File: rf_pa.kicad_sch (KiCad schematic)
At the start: 57 parts, among them J1 LMT87LPM, Q1 BSS138, Q2 BSS138, Q3 NP100P04PDG, U1 LT1013DIDR, U2 LM317_SOT-223, U3 TL431, U4 RA60H3847H1

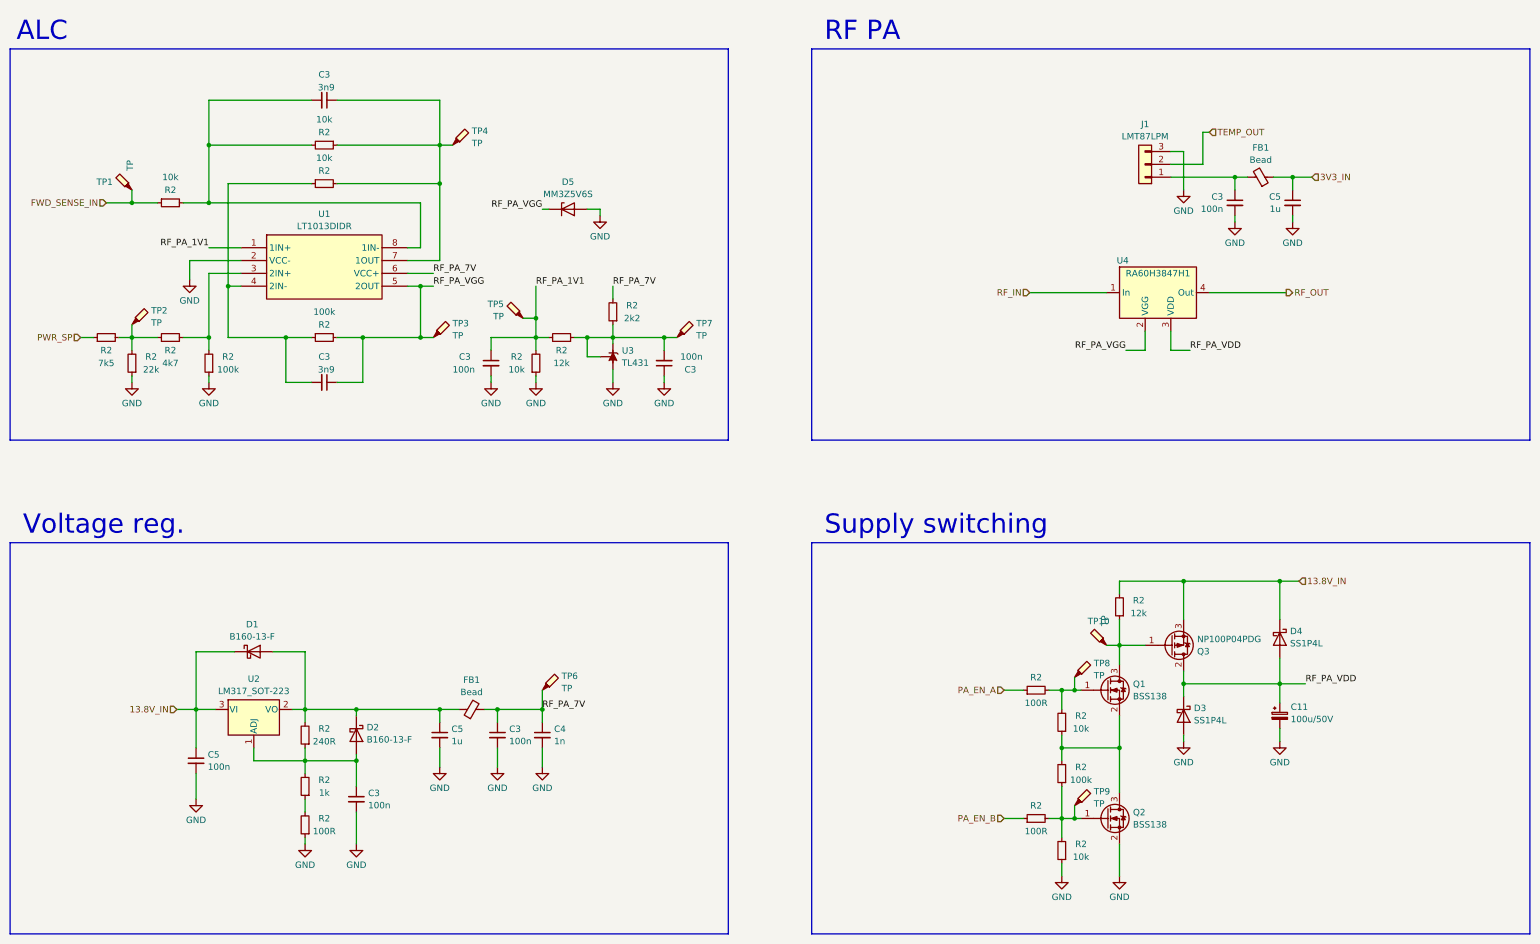
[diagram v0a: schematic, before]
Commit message: WIP rev B
- replaced R44-R46 with 22k
- exposed BOOT0 at the DA15 connector
- added a testpoint at DAC OUT2
- added a buffer to the 40MHz reference oscillator
- removed C2
- bypassed R5 with a 100nF capacitor
- changed D5's voltage to 5.1V
- routed TX_SAMP_CLK
- changed temperature sensor's supply voltage to 5V
- added a series of 100p, 1n and 10n capacitors at PA_VGG
- reduced N-connector cutouts to 2.5mm
- improved RF output track a little
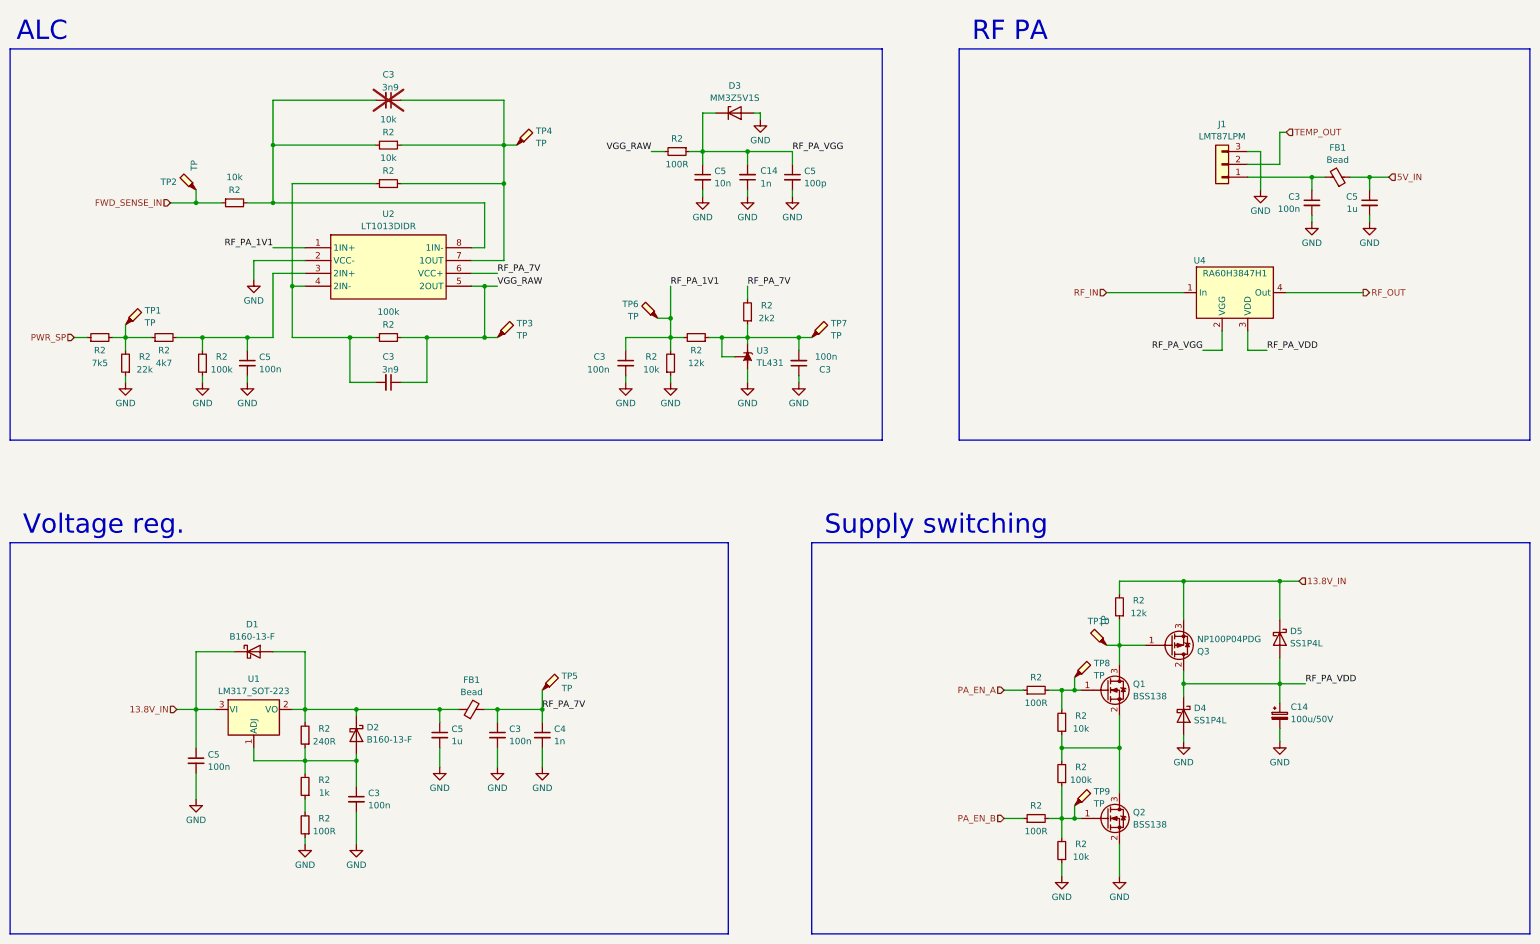
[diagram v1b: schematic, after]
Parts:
- added C14: 1n, Capacitor_SMD:C_0603_1608Metric, symbol Device:C_Small
- added C5: 10n, Capacitor_SMD:C_0603_1608Metric, symbol Device:C_Small
- added C5: 100p, Capacitor_SMD:C_0603_1608Metric, symbol Device:C_Small
- added C5: 100n, Capacitor_SMD:C_0603_1608Metric, symbol Device:C_Small
- added R2: 100R, Resistor_SMD:R_0603_1608Metric, symbol Device:R_Small
- C3: now not fitted; now left out of the parts list
- D3: renamed from D5; value MM3Z5V6S -> MM3Z5V1S; MPN MM3Z5V6ST1G -> 863-MM3Z5V1ST1G; PN MM3Z5V6ST1G -> 863-MM3Z5V1ST1G
- renumbered C11 to C14, D3 to D4, D4 to D5, TP2 to TP1, TP1 to TP2, TP6 to TP5, TP5 to TP6, U2 to U1, U1 to U2
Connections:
- net GND: now also C14.1, C5.2, C5.2, C5.2
- net RF_PA_VGG: now also C14.2, C5.1, C5.1, R2.1; no longer C3.1, R2.2, TP3.1, U2.5 (2OUT)
- net at R2.2, R2.2, U2.3 (2IN+): now also C5.1
- net 3V3_IN renamed 5V_IN
- new net VGG_RAW: C3.1, R2.2, R2.2, TP3.1, U2.5 (2OUT)
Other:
- moved on the sheet: C3, C5, D3, FB1, J1, R2, TP1, TP2, TP3, TP4, TP6, TP7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

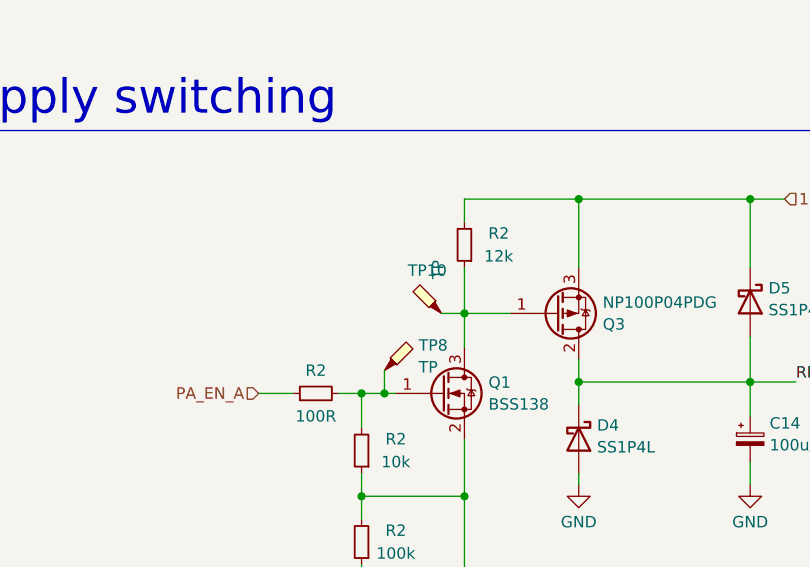
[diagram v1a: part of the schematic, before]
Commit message: routed the 40MHz oscillator
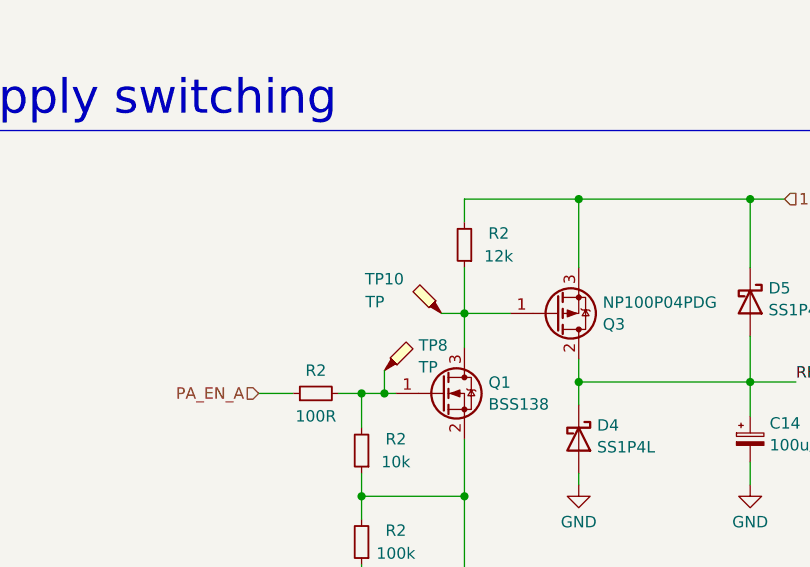
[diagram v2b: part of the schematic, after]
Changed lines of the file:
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@@
   )
   (symbol (lib_id "Connector:TestPoint_Probe") (at 271.78 175.26 90) (unit 1)
-    (in_bom yes) (on_board yes) (dnp no) (fields_autoplaced)
-    (property "Reference" "TP10" (at 270.1925 170.4919 90)
+    (in_bom yes) (on_board yes) (dnp no)
+    (property "Reference" "TP10" (at 265.43 171.45 90)
       (effects (font (size 1.27 1.27)))
     )
-    (property "Value" "TP" (at 271.4046 171.45 0)
+    (property "Value" "TP" (at 265.43 173.99 90)
       (effects (font (size 1.27 1.27)) (justify left))
     )

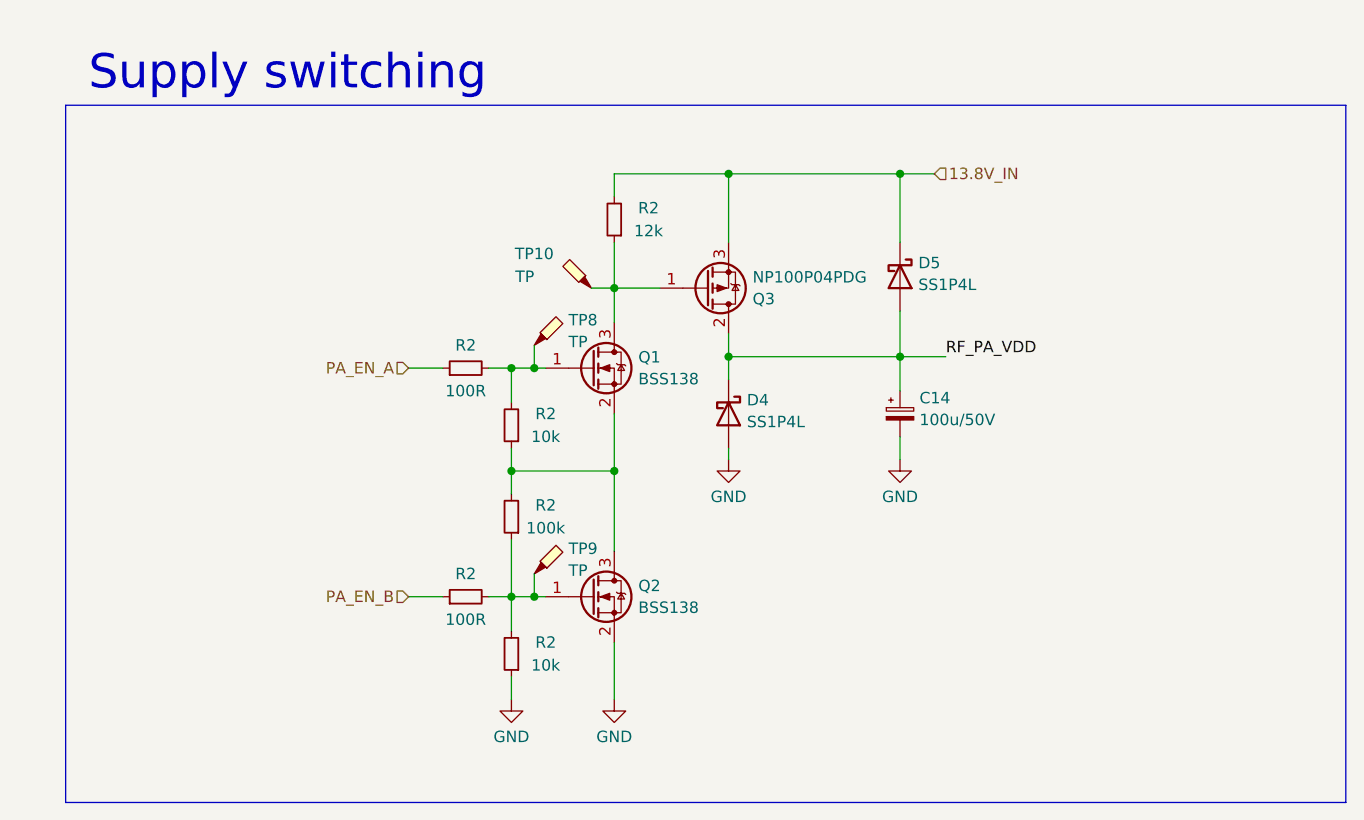
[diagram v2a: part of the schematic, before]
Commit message: WIP rev B
- added bleed resistors
- power supply now uses linear regulators
- routed RX_SAMP_CLK
- added some decoupling at RF_PA_VDD
- added some GND vias here and there
- updated BOM
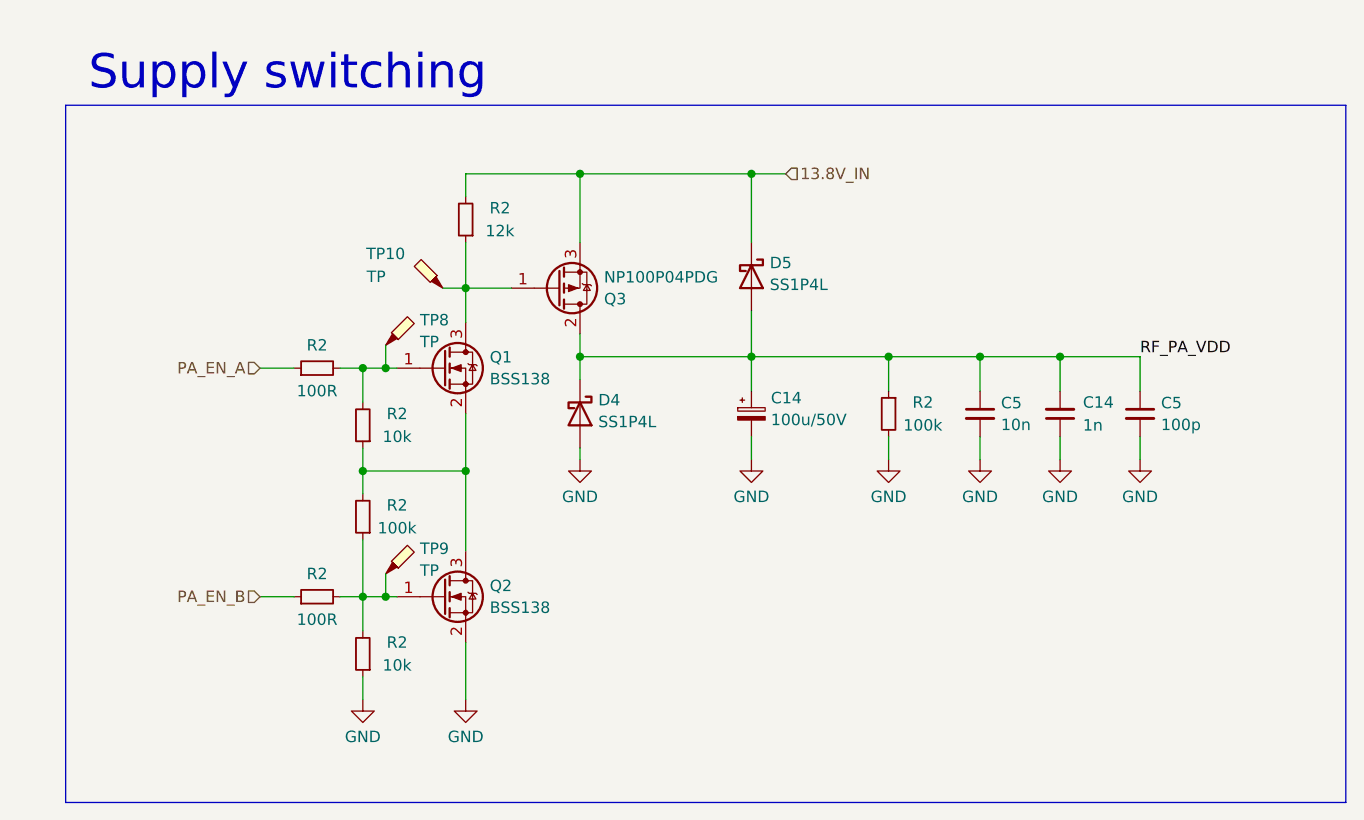
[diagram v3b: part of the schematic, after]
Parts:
- added C14: 1n, Capacitor_SMD:C_0603_1608Metric, symbol Device:C_Small
- added C5: 100p, Capacitor_SMD:C_0603_1608Metric, symbol Device:C_Small
- added C5: 10n, Capacitor_SMD:C_0603_1608Metric, symbol Device:C_Small
- added R2: 100k, Resistor_SMD:R_0603_1608Metric, symbol Device:R_Small
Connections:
- net GND: now also C14.1, C5.2, C5.2, R2.2
- net RF_PA_VDD: now also C14.2, C5.1, C5.1, R2.1
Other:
- moved on the sheet: C14, D4, D5, Q1, Q2, Q3, R2, TP10, TP8, TP9

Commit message: updated PCB render
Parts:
- D3: MPN 863-MM3Z5V1ST1G -> 863-MM3Z5V1ST1G; PN 863-MM3Z5V1ST1G -> 863-MM3Z5V1ST1G
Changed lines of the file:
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@@
       (effects (font (size 1.27 1.27)) hide)
     )
-    (property "PN" "863-MM3Z5V1ST1G " (at 198.12 69.85 0)
+    (property "PN" "863-MM3Z5V1ST1G" (at 198.12 69.85 0)
       (effects (font (size 1.27 1.27)) hide)
     )
-    (property "MPN" "863-MM3Z5V1ST1G " (at 198.12 69.85 0)
+    (property "MPN" "863-MM3Z5V1ST1G" (at 198.12 69.85 0)
       (effects (font (size 1.27 1.27)) hide)
     )

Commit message: minor footprint updates
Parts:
- D4, D5: footprint Mine:D0-220AA-SMP -> Mine:DO-220AA-SMP
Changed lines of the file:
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@@
   (title_block
     (title "Remote Radio Unit - RF board")
-    (date "19-01-2024")
+    (date "20-01-2024")
     (rev "B")
     (company "M17 Project")
@@
       (effects (font (size 1.27 1.27)) (justify left))
     )
-    (property "Footprint" "Mine:D0-220AA-SMP" (at 289.56 173.99 0)
+    (property "Footprint" "Mine:DO-220AA-SMP" (at 289.56 173.99 0)
       (effects (font (size 1.27 1.27)) hide)
     )
@@
       (effects (font (size 1.27 1.27)) (justify left))
     )
-    (property "Footprint" "Mine:D0-220AA-SMP" (at 270.51 189.23 0)
-      (effects (font (size 1.27 1.27)) hide)
-    )
+    (property "Footprint" "Mine:DO-220AA-SMP" (at 270.51 189.23 0)
+      (effects (font (size 1.27 1.27)) hide)
+    )

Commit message: minor changes
footprint name change
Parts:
- U2: footprint SOIC127P600X175-8N -> Mine:SOIC127P600X175-8N
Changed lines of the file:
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@@
       (effects (font (size 1.27 1.27)))
     )
-    (property "Footprint" "SOIC127P600X175-8N" (at 142.24 191.44 0)
+    (property "Footprint" "Mine:SOIC127P600X175-8N" (at 142.24 191.44 0)
       (effects (font (size 1.27 1.27)) (justify left top) hide)
     )

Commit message: WIP rev C
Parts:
- added C17, C18, C20, C21, C24, C25: TBF, Capacitor_SMD:C_1206_3216Metric_Pad1.33x1.80mm_HandSolder, symbol Device:C_Small
- added L1: 24nH, Parts:aircoil_L, symbol Parts:aircoil
- added L2: 24nH, Parts:aircoil_R, symbol Parts:aircoil
- renumbered C5 to C1, C5 to C10, C14 to C11, C5 to C12, C3 to C13, C3 to C14, C5 to C15, C14 to C16, C5 to C19, C5 to C2, C14 to C22, C5 to C23, C3 to C4, C3 to C5, C5 to C6, C3 to C7, C4 to C8, C3 to C9, FB1 to FB2, R2 to R1, R2 to R10, R2 to R11, R2 to R12, R2 to R13, R2 to R14, R2 to R15, R2 to R16, R2 to R17, R2 to R18, R2 to R19, R2 to R20, R2 to R21, R2 to R22, R2 to R3, R2 to R4, R2 to R5, R2 to R6, R2 to R7, R2 to R8, R2 to R9
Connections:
- net GND: now also C17.1, C18.2, C20.1, C21.2, C24.1, C25.2
- net RF_OUT: now also C24.2, C25.1, L2.2; no longer U4.4 (Out)
- new net PA_OUT: C17.2, C18.1, L1.1, U4.4 (Out)
- new net PA_OUT_2: C20.2, C21.1, L1.2, L2.1
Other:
- note added: "To be populated manually later on"
- moved on the sheet: C14, C15, FB2, J1, U4

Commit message: WIP rev C
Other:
- note added: "Aircoils: 0.8mm silver plated copper wire 3 turns 3.2mm inner dia ~4mm length Resulting inductance should be around 24nH"
- note added: "Caps to be populated manually later on"
- note removed: "To be populated manually later on"
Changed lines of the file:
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@@
   (title_block
     (title "Remote Radio Unit - RF board")
-    (date "04-04-2024")
+    (date "05-04-2024")
     (rev "C")
     (company "M17 Project")
@@
     (effects (font (size 3.81 3.81)) (justify left bottom))
   )
-  (text "To be populated manually later on" (at 303.53 87.63 0)
+  (text "Caps to be populated manually later on" (at 300.99 127 0)
     (effects (font (size 1.27 1.27)) (justify left bottom))
   )
+  (text "Aircoils:\n0.8mm silver plated copper wire\n3 turns\n3.2mm inner dia\n~4mm length\nResulting inductance should be around 24nH"
+    (at 300.99 85.09 0)
+    (effects (font (size 1.27 1.27)) (justify left bottom))
+  )
